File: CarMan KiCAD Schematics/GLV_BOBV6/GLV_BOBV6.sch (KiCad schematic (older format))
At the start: 24 parts, among them J1 2PinPortRight, J10 2PinPortRight, J2 2PinPortRight, J4 4PinPort, J5 2PinPortRight, J7 2PinPortRight, J8 2PinPortRight, U1 DCR012405U

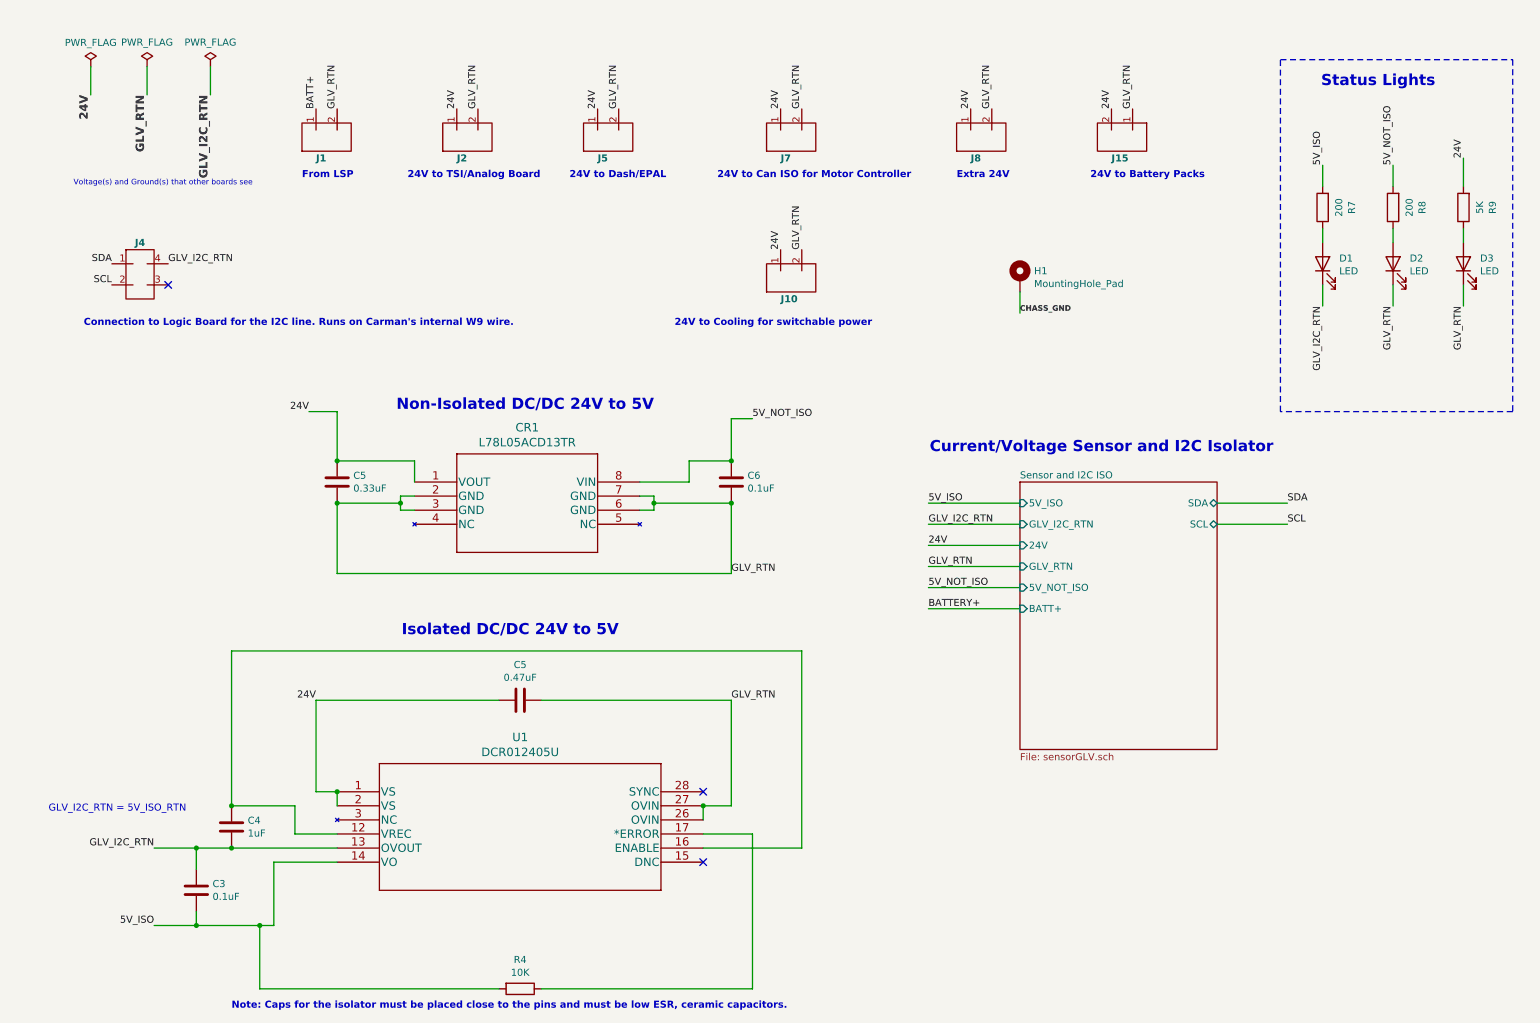
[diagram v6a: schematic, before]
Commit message: Updated GLV with breaker connectors and connections, changed I2C PU resistors, added remaining pwr flags.
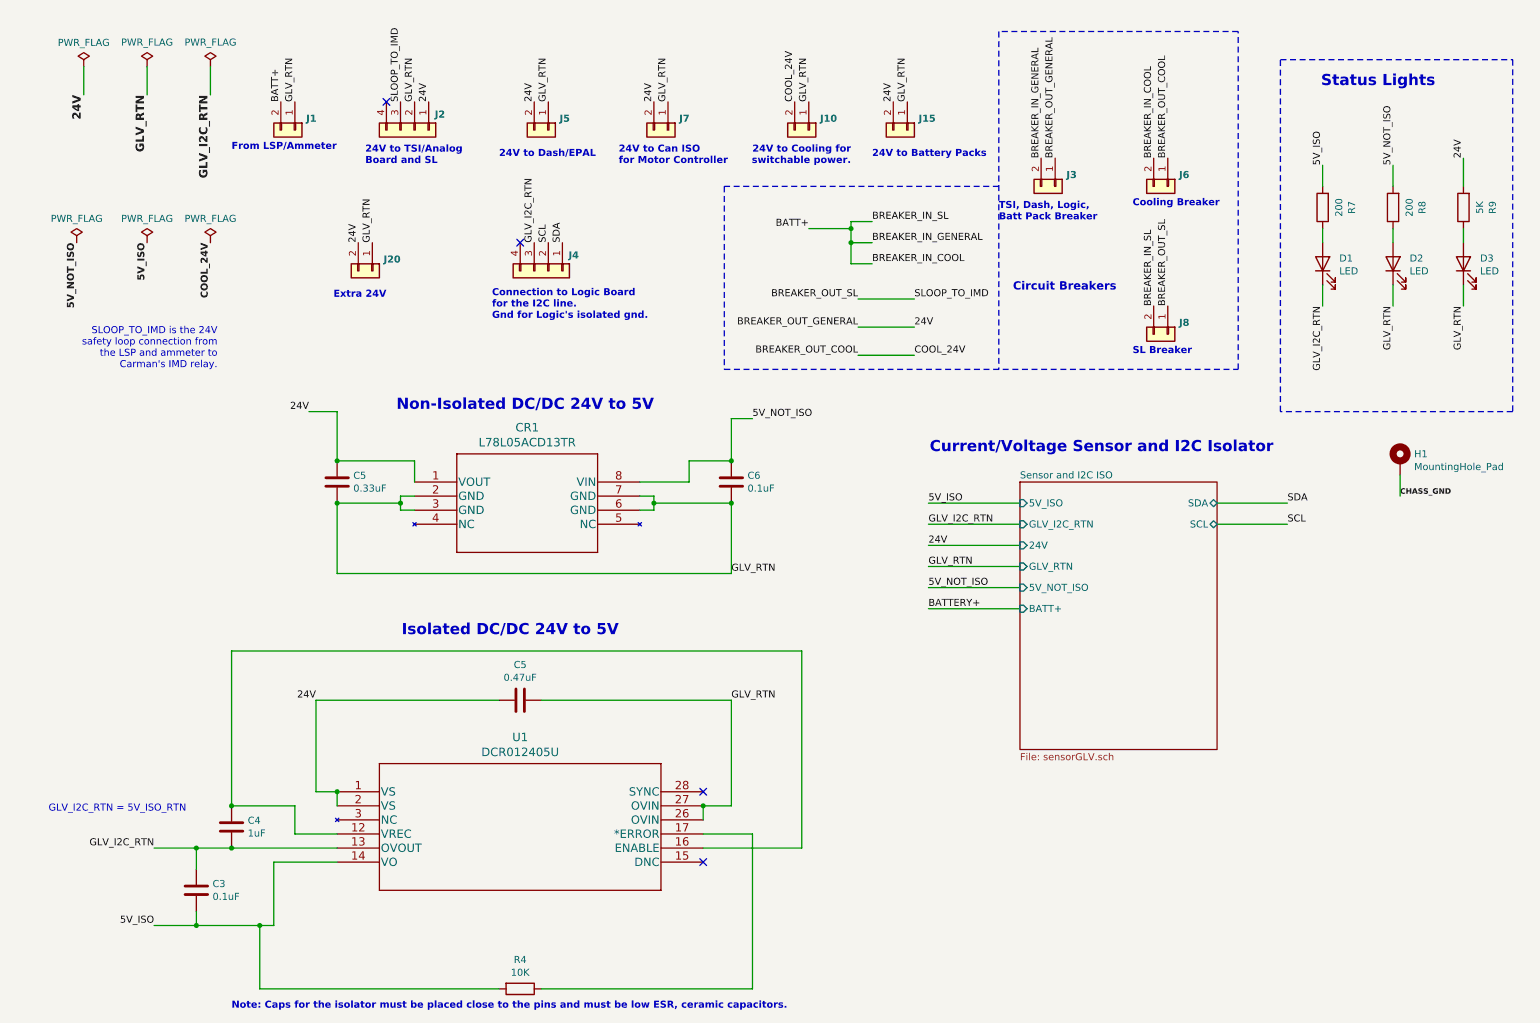
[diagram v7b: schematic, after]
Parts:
- removed J1, J10, J2, J5, J7, J8: 2PinPortRight, symbol CarMan_KiCAD_Library:2PinPortRight
- removed J4: 4PinPort, symbol CarMan_KiCAD_Library:4PinPort
- removed U?: J15, symbol CarMan_KiCAD_Library:2PinPortLeft
- added 24V? (x3): PWR_FLAG, symbol power:PWR_FLAG
- added J1, J10, J15, J20, J3, J5, J6, J7, J8: Conn_01x02, symbol Connector_Generic:Conn_01x02
- added J2, J4: Conn_01x04, symbol Connector_Generic:Conn_01x04
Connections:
- net 24V: now also J15.2 (Pin_2), J2.1 (Pin_1), J20.2 (Pin_2), J3.1 (Pin_1), J5.2 (Pin_2), J7.2 (Pin_2)
- net 5V_ISO: now also 24V?.1 (pwr)
- net 5V_NOT_ISO: now also 24V?.1 (pwr)
- net BATT+: now also J1.2 (Pin_2), J3.2 (Pin_2), J6.2 (Pin_2), J8.2 (Pin_2)
- net GLV_I2C_RTN: now also J4.3 (Pin_3)
- net GLV_RTN: now also J1.1 (Pin_1), J10.1 (Pin_1), J15.1 (Pin_1), J2.2 (Pin_2), J20.1 (Pin_1), J5.1 (Pin_1), J7.1 (Pin_1)
- net SCL: now also J4.2 (Pin_2)
- net SDA: now also J4.1 (Pin_1)
- new net BREAKER_OUT_COOL: 24V?.1 (pwr), J10.2 (Pin_2), J6.1 (Pin_1)
- new net BREAKER_OUT_SL: J2.3 (Pin_3), J8.1 (Pin_1)
- no-connect marks 3 -> 4
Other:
- note added: "24V to Can ISO\nfor Motor Controller"
- note added: "24V to Cooling for\nswitchable power."
- note added: "24V to TSI/Analog\nBoard and SL"
- note added: "Circuit Breakers"
- note added: "Connection to Logic Board\nfor the I2C line. \nGnd for Logic's isolated gnd."
- note added: "Cooling Breaker"
- note added: "Extra 24V"
- note added: "From LSP/Ammeter"
- note added: "SL Breaker\n"
- note added: "SLOOP_TO_IMD is the 24V \nsafety loop connection from \nthe LSP and ammeter to \nCarman's IMD relay."
- note added: "TSI, Dash, Logic,\nBatt Pack Breaker"
- note removed: "24V to Can ISO for Motor Controller"
- note removed: "24V to Cooling for switchable power"
- note removed: "24V to TSI/Analog Board"
- note removed: "Connection to Logic Board for the I2C line. Runs on Carman's internal W9 wire."
- note removed: "Extra 24V\n"
- note removed: "From LSP"
- note removed: "Voltage(s) and Ground(s) that other boards see"
- moved on the sheet: H1

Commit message: GLV with updated connector names, removed isolated converter and I2C isolator
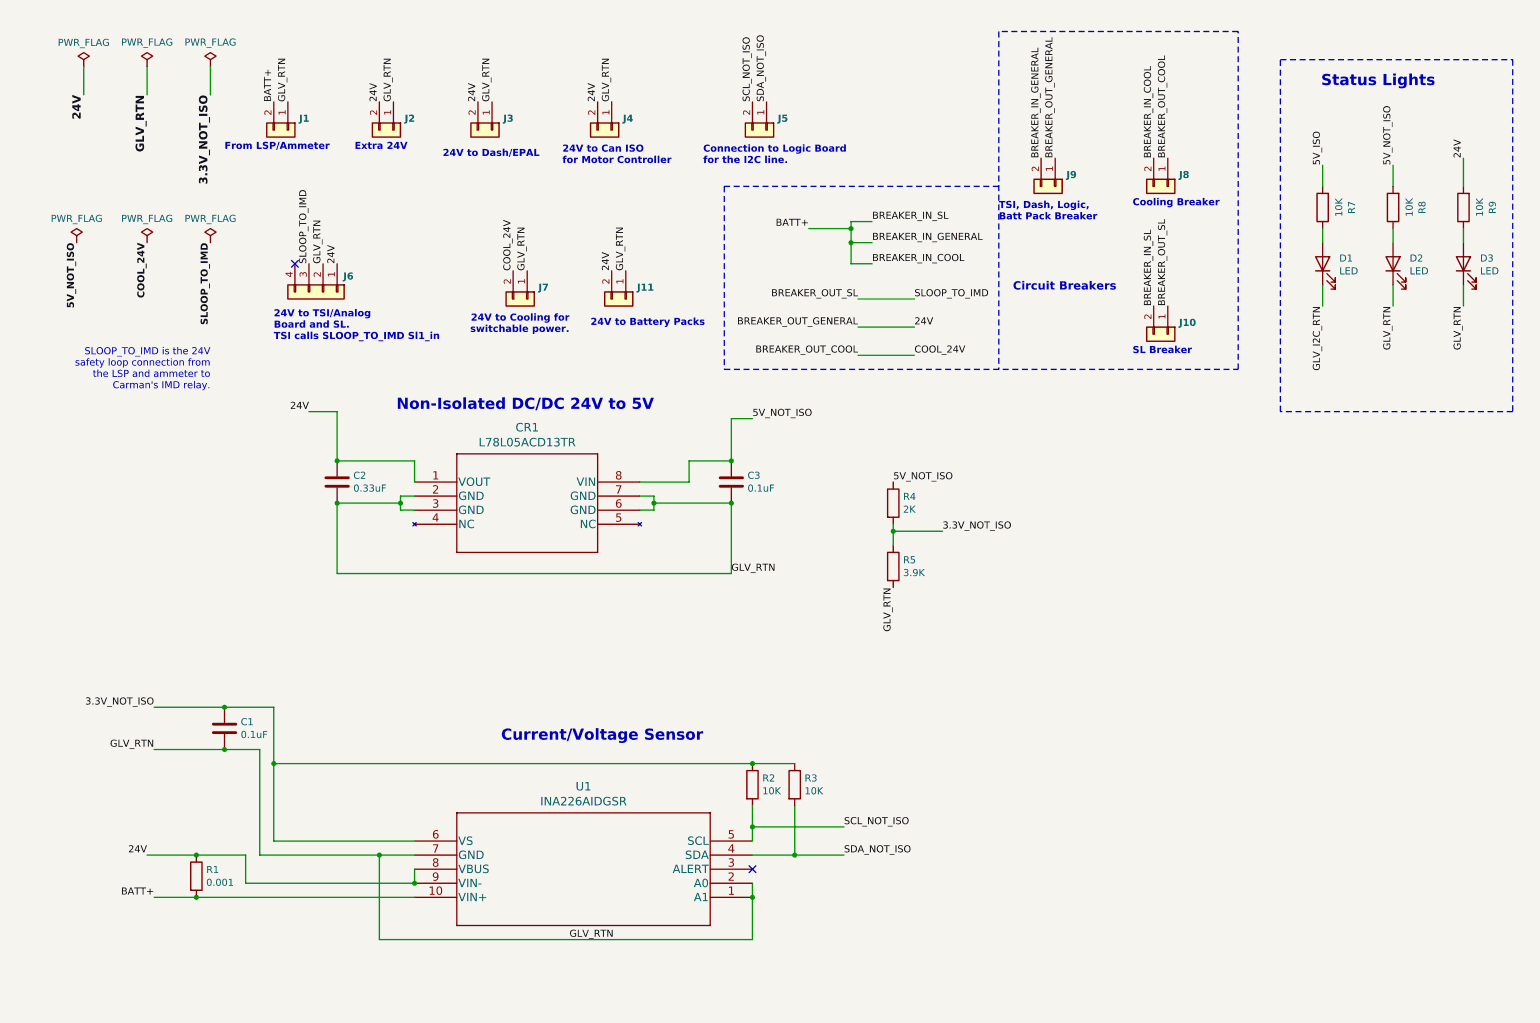
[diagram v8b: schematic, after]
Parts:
- removed 24V?: PWR_FLAG, symbol power:PWR_FLAG
- removed C3: 0.1uF, symbol Device:C
- removed C4: 1uF, symbol Device:C
- removed C5: 0.47uF, symbol Device:C
- removed H1: MountingHole_Pad, symbol Mechanical:MountingHole_Pad
- removed J4: Conn_01x04, symbol Connector_Generic:Conn_01x04
- removed U1: DCR012405U, DVB12, symbol CarMan_KiCAD_Library:DCR012405U
- added 24V04: PWR_FLAG, symbol power:PWR_FLAG
- added C1: 0.1uF, symbol Device:C
- added J5: Conn_01x02, symbol Connector_Generic:Conn_01x02
- added R1: 0.001, symbol Device:R
- added R2, R3: 10K, symbol Device:R
- added R5: 3.9K, symbol Device:R
- added U1: INA226AIDGSR, DGS10, symbol CarMan_KiCAD_Library:INA226AIDGSR
- R4: value 10K -> 2K
- R7, R8: value 200 -> 10K
- R9: value 5K -> 10K
- gave numbers to parts that had none: 2
- renumbered 24V to 24V02, C5 to C2, C6 to C3, J8 to J10, J15 to J11, J20 to J2, J5 to J3, J7 to J4, J2 to J6, J10 to J7, J6 to J8, J3 to J9
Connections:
- net 24V: now also R1.1, U1.8 (VBUS), U1.9 (VIN-)
- net 5V_ISO: no longer R4.2
- net 5V_NOT_ISO: now also R4.1
- net BATT+: now also R1.2, U1.10 (VIN+)
- net BREAKER_OUT_SL: now also 24V04.1 (pwr)
- net GLV_RTN: now also C1.2, R5.2, U1.1 (A1), U1.2 (A0), U1.7 (GND)
- new net 3.3V_NOT_ISO: C1.1, R2.1, R3.1, R4.2, R5.1, U1.6 (VS)
- new net SCL_NOT_ISO: J5.2 (Pin_2), R2.2, U1.5 (SCL)
- new net SDA_NOT_ISO: J5.1 (Pin_1), R3.2, U1.4 (SDA)
- no-connect marks 4 -> 2
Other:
- note added: "24V to TSI/Analog\nBoard and SL. \nTSI calls SLOOP_TO_IMD Sl1_in"
- note added: "Connection to Logic Board\nfor the I2C line. \n"
- note added: "Current/Voltage Sensor"
- note removed: "24V to TSI/Analog\nBoard and SL"
- note removed: "Connection to Logic Board\nfor the I2C line. \nGnd for Logic's isolated gnd."
- note removed: "Current/Voltage Sensor and I2C Isolator"
- note removed: "GLV_I2C_RTN = 5V_ISO_RTN"
- note removed: "Isolated DC/DC 24V to 5V"
- note removed: "Note: Caps for the isolator must be placed close to the pins and must be low ESR, ceramic capacitors."
- moved on the sheet: J1, J11, J2, J3, J4, J6, J7
